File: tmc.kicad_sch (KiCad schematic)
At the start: 33 parts, among them J3 Screw_Terminal_01x04, Q2 CSD18533Q5A, Q3 CSD18533Q5A, Q4 CSD18533Q5A, Q5 CSD18533Q5A, Q6 CSD18533Q5A, Q7 CSD18533Q5A, Q8 CSD18533Q5A, Q9 CSD18533Q5A, U3 TMC5160A-TA

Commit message: Lots of work
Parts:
- removed Q2, Q3, Q4, Q5, Q6, Q7, Q8, Q9: CSD18533Q5A, Package_TO_SOT_SMD:TDSON-8-1, symbol Transistor_FET:CSD18533Q5A
- added Q14, Q2, Q37, Q6: ~, easyeda2kicad:POWERPAK-SO-8_L6.2-W5.2-P1.27-BL_POWERPAK, symbol FET:SQJB70EP-T1_GE3
- D10: renamed from D7; footprint LED_SMD:LED_WS2812B-2020_PLCC4_2.0x2.0mm -> LED_SMD:LED_WS2812B-Mini_PLCC4_3.5x3.5mm; symbol LED:WS2812B-2020 -> LED:WS2812B; Part (none) -> 2659 (adafruit)
- R34: renamed from R13; footprint Resistor_SMD:R_1206_3216Metric -> Resistor_SMD:R_2512_6332Metric; Part RL1206FR-070R075L -> CRA2512-FZ-R075ELF
- R37: renamed from R16; footprint Resistor_SMD:R_1206_3216Metric -> Resistor_SMD:R_2512_6332Metric; Part RL1206FR-070R075L -> CRA2512-FZ-R075ELF
- renumbered C12 to C54, C13 to C55, C14 to C56, C15 to C57, C16 to C58, C17 to C59, C18 to C60, C19 to C61, C20 to C62, C21 to C63, C22 to C64, C23 to C65, C24 to C66, C25 to C67, J3 to J7, JP2 to JP13, R10 to R31, R11 to R32, R12 to R33, R14 to R35, R15 to R36, U3 to U6
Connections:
- net BMA1: now also J7.2 (Pin_2), Q14.2 (S1), Q2.5 (D1); no longer J7.1 (Pin_1)
- net BMA2: now also J7.1 (Pin_1), Q14.3 (S2), Q2.6 (D2); no longer J7.2 (Pin_2)
- net BMB1: now also J7.4 (Pin_4), Q37.2 (S1), Q6.5 (D1); no longer J7.3 (Pin_3)
- net BMB2: now also J7.3 (Pin_3), Q37.3 (S2), Q6.6 (D2); no longer J7.4 (Pin_4)
- net GND: now also D10.3 (VSS); no longer D10.2 (VSS)
- net HA1: now also Q14.1 (G1)
- net HA2: now also Q14.4 (G2)
- net HB1: now also Q37.1 (G1)
- net HB2: now also Q37.4 (G2)
- net LA1: now also Q2.1 (G1)
- net LA2: now also Q2.4 (G2)
- net LB1: now also Q6.1 (G1)
- net LB2: now also Q6.4 (G2)
- net LED_IN: now also D10.4 (DIN); no longer D10.3 (DIN)
- net LED_OUT: now also D10.2 (DOUT); no longer D10.1 (DOUT)
- net SA: now also Q2.2 (S1), Q2.3 (S2); no longer R35.1, R37.1
- net VLED: now also D10.1 (VDD); no longer D10.4 (VDD)
- net VMOT: now also Q14.5 (D1), Q14.6 (D2), Q37.5 (D1), Q37.6 (D2)
- new net SB: Q6.2 (S1), Q6.3 (S2), R35.1, R37.1
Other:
- moved on the sheet: C61, C62, C63, C64, C65, C66, C67, D10, R32, R33, R34, R35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

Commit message: first stepper unit
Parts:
- removed Q14, Q2, Q37, Q6: ~, easyeda2kicad:POWERPAK-SO-8_L6.2-W5.2-P1.27-BL_POWERPAK, symbol FET:SQJB70EP-T1_GE3
- added Q10, Q14, Q2, Q26, Q27, Q3, Q6, Q7: Q_NMOS_DGS, FET:Diodes_DMT6016LFDF, symbol Device:Q_NMOS_DGS
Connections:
- net BMA1: now also Q14.3 (S), Q2.1 (D)
- net BMA2: now also Q10.3 (S), Q3.1 (D)
- net BMB1: now also Q26.1 (D), Q6.3 (S)
- net BMB2: now also Q27.1 (D), Q7.3 (S)
- net HA1: now also Q14.2 (G)
- net HA2: now also Q10.2 (G)
- net HB1: now also Q6.2 (G)
- net HB2: now also Q7.2 (G)
- net LA1: now also Q2.2 (G)
- net LA2: now also Q3.2 (G)
- net LB1: now also Q26.2 (G)
- net LB2: now also Q27.2 (G)
- net SA: now also Q2.3 (S), Q3.3 (S)
- net SB: now also Q26.3 (S), Q27.3 (S)
- net VMOT: now also Q10.1 (D), Q14.1 (D), Q6.1 (D), Q7.1 (D)

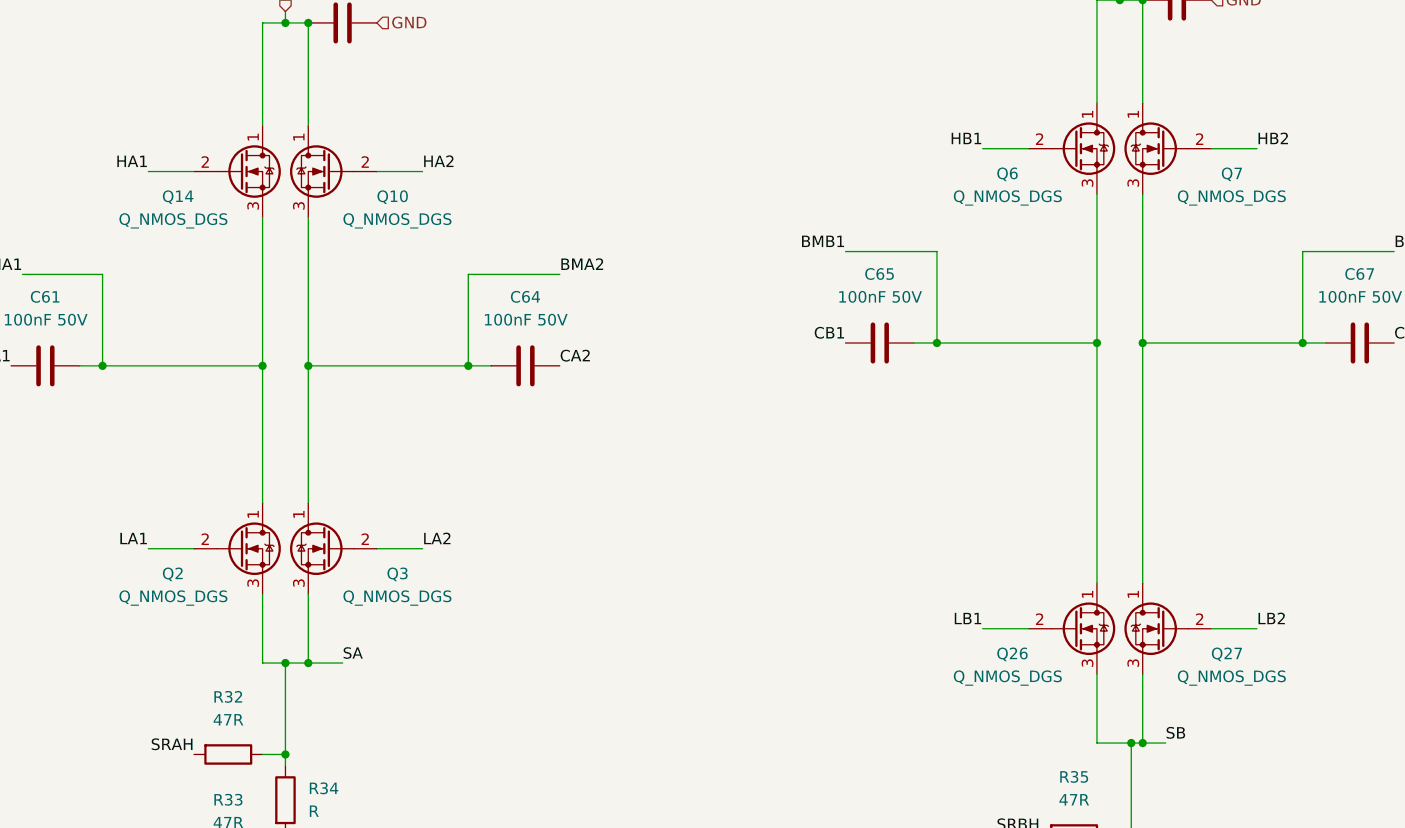
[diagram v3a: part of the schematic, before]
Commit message: stepper unit 2 and 3, begin work on unit 4
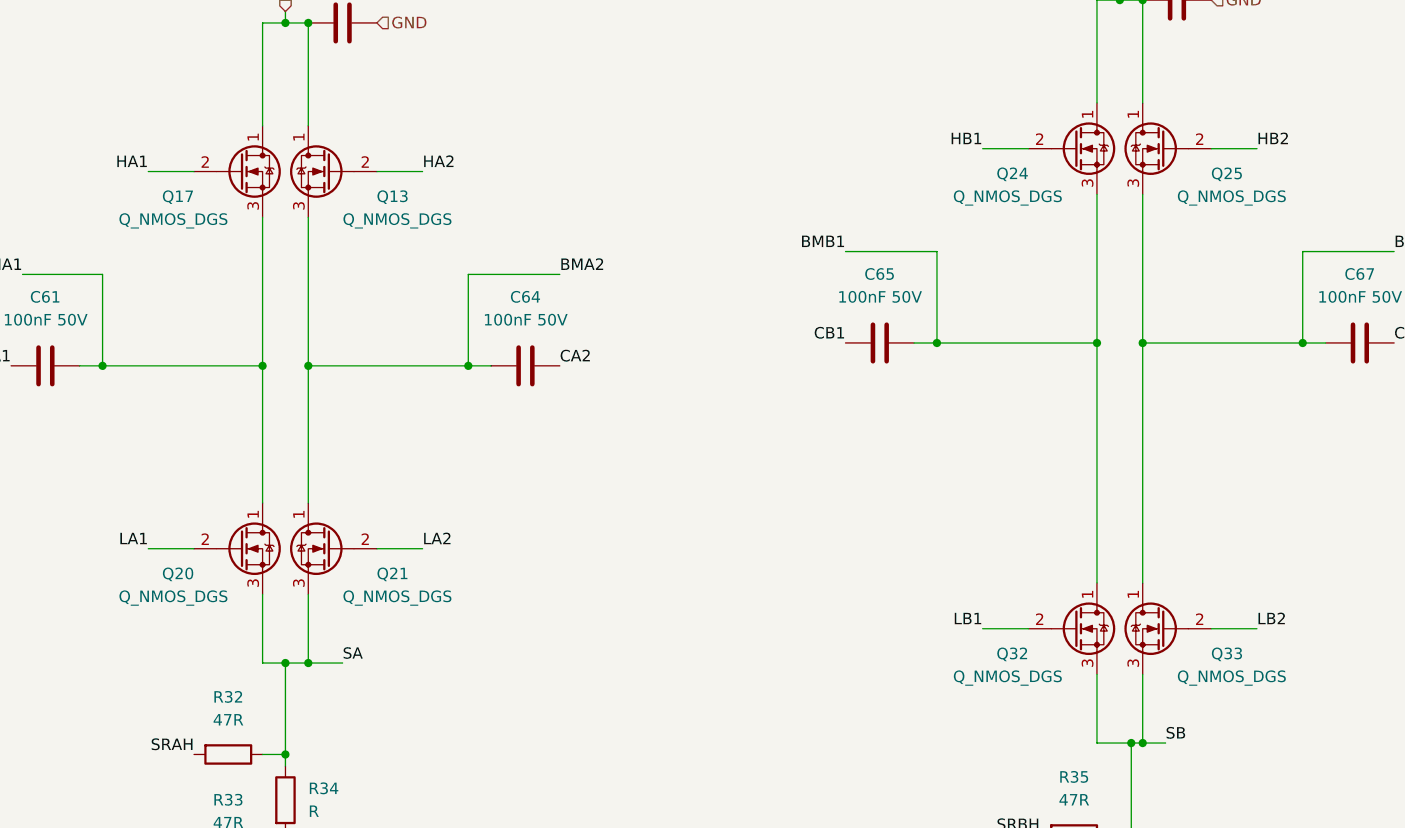
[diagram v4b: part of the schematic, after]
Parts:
- U6: footprint Package_QFP:TQFP-48-1EP_7x7mm_P0.5mm_EP5x5mm_ThermalVias -> QFP_Thermal:TQFP-48-1EP_7x7mm_P0.5mm_EP5x5mm_ThermalVias_0.3
- renumbered Q10 to Q13, Q14 to Q17, Q2 to Q20, Q3 to Q21, Q6 to Q24, Q7 to Q25, Q26 to Q32, Q27 to Q33
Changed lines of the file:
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@@
 		(on_board yes)
 		(dnp no)
-		(property "Reference" "Q7"
+		(property "Reference" "Q25"
 			(at 256.286 53.594 0)
 			(effects
@@
 		(on_board yes)
 		(dnp no)
-		(property "Reference" "Q26"
+		(property "Reference" "Q32"
 			(at 228.854 106.934 0)
 			(effects
@@
 		(on_board yes)
 		(dnp no)
-		(property "Reference" "Q14"
+		(property "Reference" "Q17"
 			(at 136.144 56.134 0)
 			(effects
@@
 		(on_board yes)
 		(dnp no)
-		(property "Reference" "Q10"
+		(property "Reference" "Q13"
 			(at 163.576 56.134 0)
 			(effects
@@
 		(on_board yes)
 		(dnp no)
-		(property "Reference" "Q6"
+		(property "Reference" "Q24"
 			(at 228.854 53.594 0)
 			(effects
@@
 		(on_board yes)
 		(dnp no)
-		(property "Reference" "Q3"
+		(property "Reference" "Q21"
 			(at 163.576 98.044 0)
 			(effects
@@
 		(on_board yes)
 		(dnp no)
-		(property "Reference" "Q27"
+		(property "Reference" "Q33"
 			(at 256.286 106.934 0)
 			(effects
@@
 			)
 		)
-		(property "Footprint" "Package_QFP:TQFP-48-1EP_7x7mm_P0.5mm_EP5x5mm_ThermalVias"
+		(property "Footprint" "QFP_Thermal:TQFP-48-1EP_7x7mm_P0.5mm_EP5x5mm_ThermalVias_0.3"
 			(at 77.47 143.51 0)
 			(effects
@@
 		(on_board yes)
 		(dnp no)
-		(property "Reference" "Q2"
+		(property "Reference" "Q20"
 			(at 136.144 98.044 0)
 			(effects

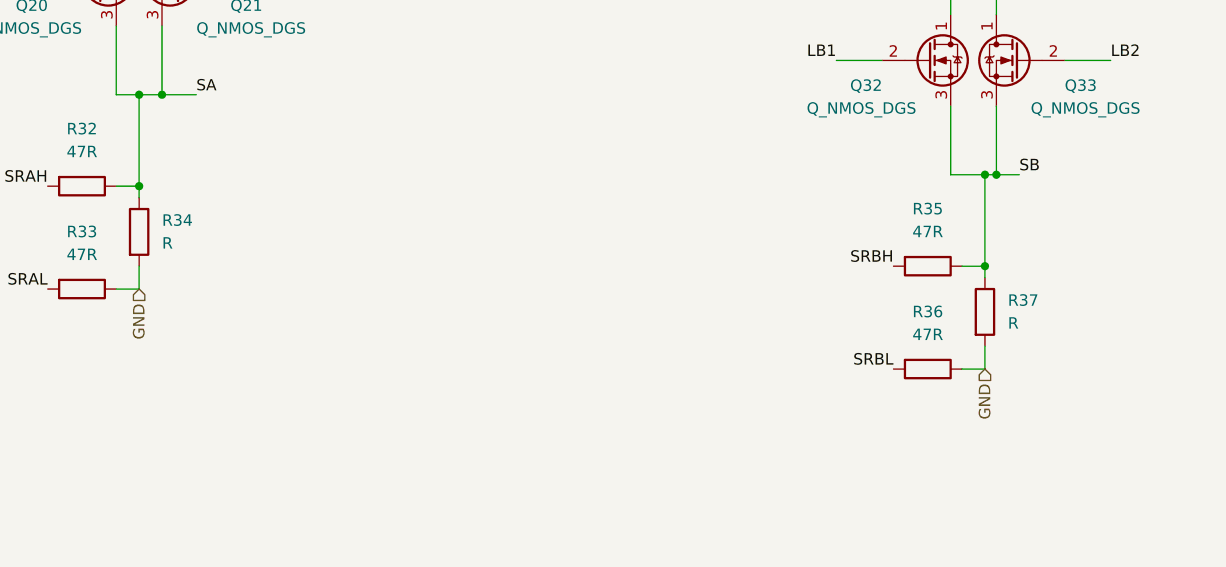
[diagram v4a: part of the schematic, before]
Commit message: Updated footprints, digikey parts
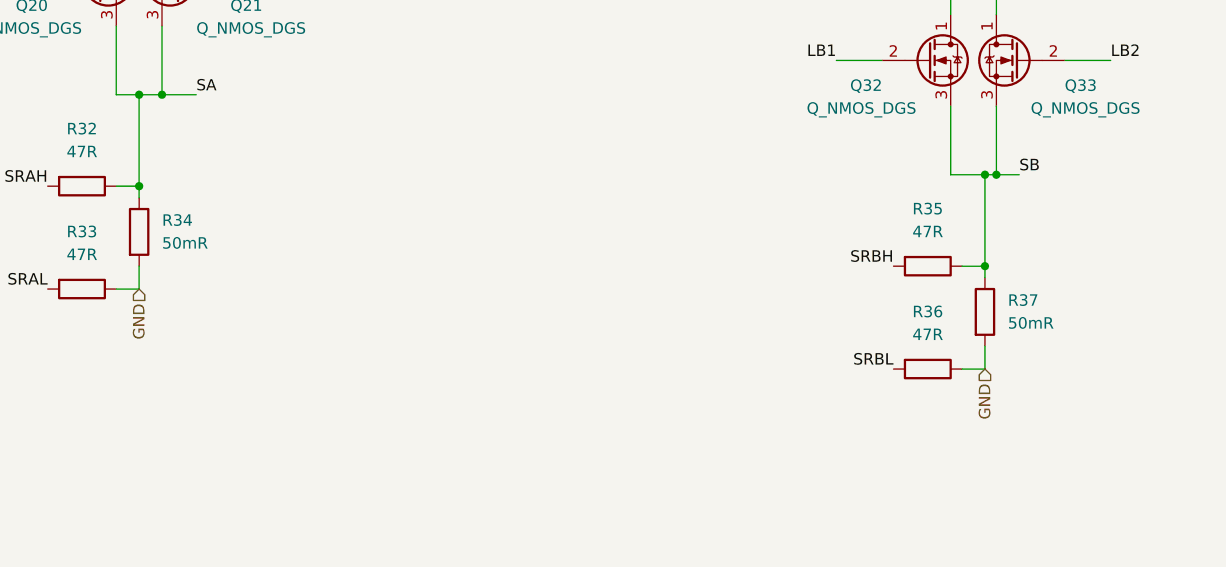
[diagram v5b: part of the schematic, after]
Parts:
- J7: Part (none) -> 1755752
- Q13, Q17, Q20, Q21, Q24, Q25, Q32, Q33: Part (none) -> DMT6016LFDF-7
- R34, R37: value R -> 50mR; Part CRA2512-FZ-R075ELF -> CRA2512-FZ-R050ELF
- U6: Part (none) -> TMC5160A-TA
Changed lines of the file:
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@@
+			)
+		)
+		(property "Part" "DMT6016LFDF-7"
+			(at 247.65 50.8 0)
+			(effects
+				(font
+					(size 1.27 1.27)
+				)
+				(hide yes)
 			)
 		)
@@
 			)
 		)
+		(property "Part" "DMT6016LFDF-7"
+			(at 237.49 104.14 0)
+			(effects
+				(font
+					(size 1.27 1.27)
+				)
+				(hide yes)
+			)
+		)
 		(pin "2"
 		)
@@
 			)
 		)
+		(property "Part" "DMT6016LFDF-7"
+			(at 144.78 53.34 0)
+			(effects
+				(font
+					(size 1.27 1.27)
+				)
+				(hide yes)
+			)
+		)
 		(pin "2"
 		)
@@
 			)
 		)
-		(property "Value" "R"
+		(property "Value" "50mR"
 			(at 152.4 124.4599 0)
 			(effects
@@
 			)
 		)
-		(property "Part" "CRA2512-FZ-R075ELF"
+		(property "Part" "CRA2512-FZ-R050ELF"
 			(at 149.86 123.19 0)
 			(effects
@@
 			)
 		)
+		(property "Part" "DMT6016LFDF-7"
+			(at 154.94 53.34 0)
+			(effects
+				(font
+					(size 1.27 1.27)
+				)
+				(hide yes)
+			)
+		)
 		(pin "2"
 		)
@@
 			)
 		)
+		(property "Part" "DMT6016LFDF-7"
+			(at 237.49 50.8 0)
+			(effects
+				(font
+					(size 1.27 1.27)
+				)
+				(hide yes)
+			)
+		)
 		(pin "2"
 		)
@@
 			)
 		)
+		(property "Part" "1755752"
+			(at 86.36 152.4 0)
+			(effects
+				(font
+					(size 1.27 1.27)
+				)
+				(hide yes)
+			)
+		)
 		(pin "1"
 		)
@@
 			)
 		)
+		(property "Part" "DMT6016LFDF-7"
+			(at 154.94 95.25 0)
+			(effects
+				(font
+					(size 1.27 1.27)
+				)
+				(hide yes)
+			)
+		)
 		(pin "2"
 		)
@@
 			)
 		)
+		(property "Part" "DMT6016LFDF-7"
+			(at 247.65 104.14 0)
+			(effects
+				(font
+					(size 1.27 1.27)
+				)
+				(hide yes)
+			)
+		)
 		(pin "2"
 		)
@@
 			)
 		)
+		(property "Part" "TMC5160A-TA"
+			(at 77.47 92.71 0)
+			(effects
+				(font
+					(size 1.27 1.27)
+				)
+				(hide yes)
+			)
+		)
 		(pin "19"
 		)
@@
 		)
 		(property "Description" "N-MOSFET transistor, drain/gate/source"
+			(at 144.78 95.25 0)
+			(effects
+				(font
+					(size 1.27 1.27)
+				)
+				(hide yes)
+			)
+		)
+		(property "Part" "DMT6016LFDF-7"
 			(at 144.78 95.25 0)
 			(effects
@@
 			)
 		)
-		(property "Value" "R"
+		(property "Value" "50mR"
 			(at 246.38 133.3499 0)
 			(effects
@@
 			)
 		)
-		(property "Part" "CRA2512-FZ-R075ELF"
+		(property "Part" "CRA2512-FZ-R050ELF"
 			(at 243.84 132.08 0)
 			(effects
